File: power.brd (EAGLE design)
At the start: 65 x 56 mm, 7 parts, among them X1 5566-4-RIGHTANGLE, X3 RASPI_BOARD_B+#_H

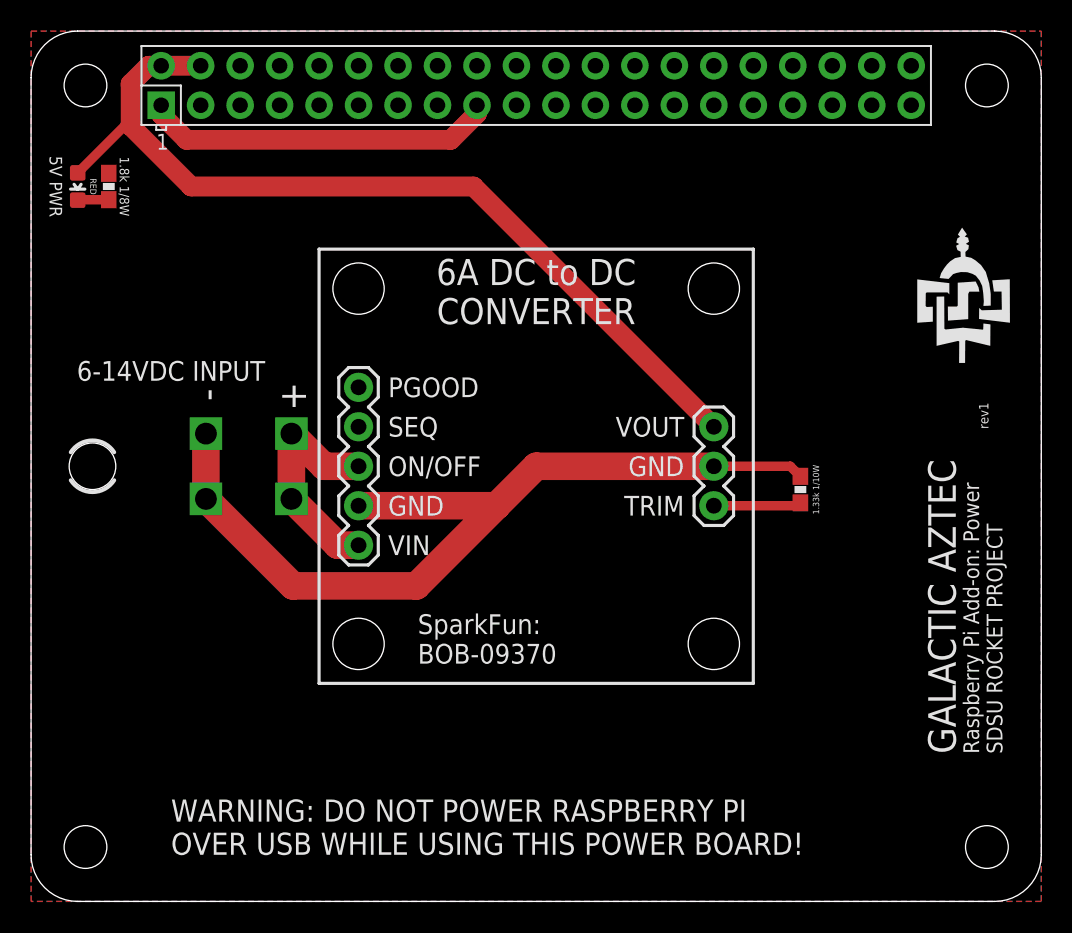
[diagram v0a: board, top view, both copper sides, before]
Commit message: Fix molex connector thru hole size
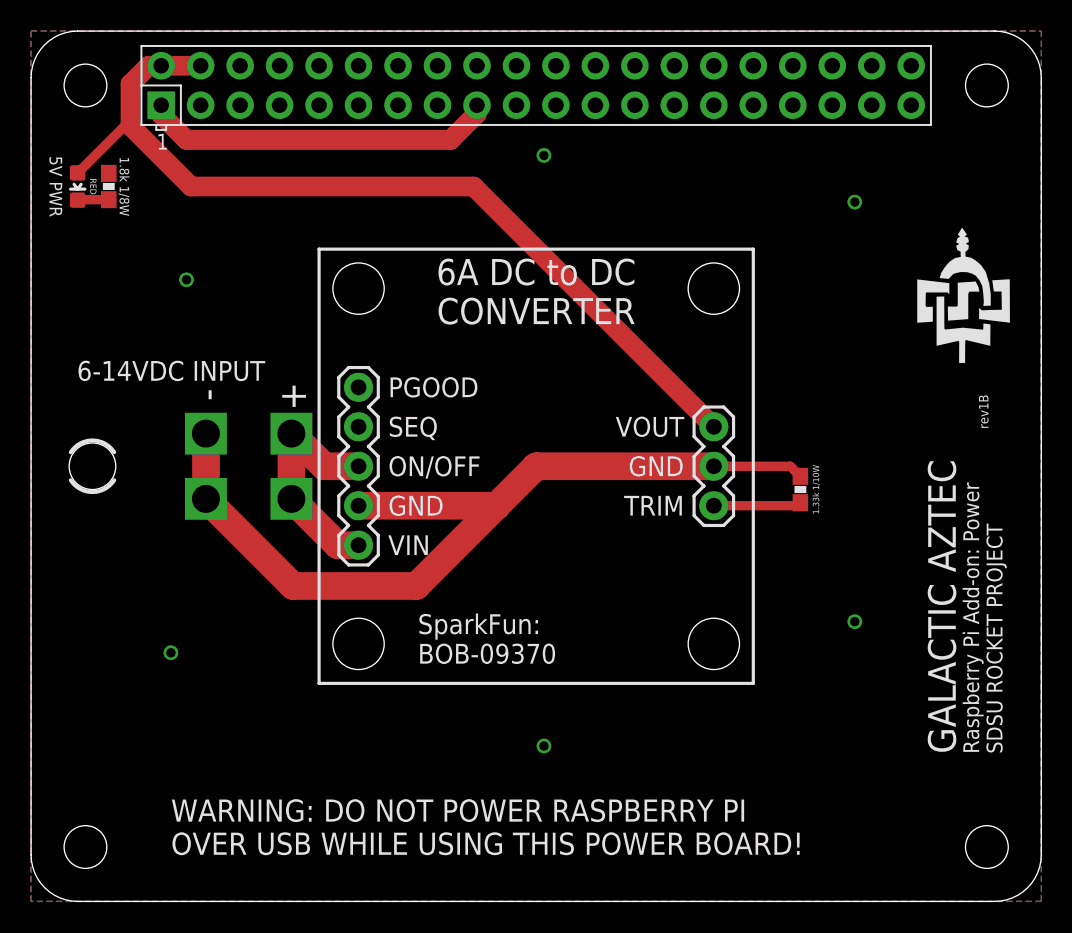
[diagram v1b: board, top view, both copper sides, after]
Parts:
- removed X1: 5566-4-RIGHTANGLE, SDSURocket-BreakoutBoards:5566-4
- added X2: 5566-4-RIGHTANGLE, SDSURocket-Connectors:5566-4
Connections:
- net GND: now also X2.1, X2.2; no longer X1.1, X1.2
- net VIN: now also X2.3, X2.4; no longer X1.3, X1.4
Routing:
- net GND: vias 0 -> 6
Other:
- board text added: "rev1B"
- board text removed: "rev1"
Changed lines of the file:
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@@
 <layer number="56" name="wert" color="7" fill="1" visible="no" active="no"/>
 <layer number="57" name="tCAD" color="7" fill="1" visible="no" active="no"/>
+<layer number="59" name="tCarbon" color="7" fill="1" visible="no" active="no"/>
+<layer number="60" name="bCarbon" color="7" fill="1" visible="no" active="no"/>
 <layer number="90" name="Modules" color="5" fill="1" visible="no" active="no"/>
 <layer number="91" name="Nets" color="2" fill="1" visible="no" active="no"/>
@@
 <layer number="127" name="_tValues" color="7" fill="1" visible="yes" active="yes"/>
 <layer number="128" name="_bValues" color="7" fill="1" visible="yes" active="yes"/>
+<layer number="129" name="Mask" color="7" fill="1" visible="yes" active="yes"/>
 <layer number="131" name="tAdjust" color="7" fill="1" visible="yes" active="yes"/>
 <layer number="132" name="bAdjust" color="7" fill="1" visible="yes" active="yes"/>
@@
 <layer number="251" name="SMDround" color="12" fill="11" visible="no" active="no"/>
 <layer number="254" name="cooling" color="7" fill="1" visible="yes" active="yes"/>
+<layer number="255" name="routoute" color="7" fill="1" visible="yes" active="yes"/>
 </layers>
 <board>
@@
 <text x="61" y="9.5" size="1.016" layer="25" font="vector" ratio="10" rot="R90">Raspberry Pi Add-on: Power</text>
 <text x="62.5" y="9.5" size="1.016" layer="25" font="vector" rot="R90">SDSU ROCKET PROJECT</text>
-<text x="61.6" y="30.4" size="0.6096" layer="25" font="vector" rot="R90">rev1</text>
+<text x="61.6" y="30.4" size="0.6096" layer="25" font="vector" rot="R90">rev1B</text>
 <text x="11.3" y="32.6" size="1.778" layer="25" font="vector" ratio="10" rot="R270" align="center">-</text>
 <text x="16.8" y="32.5" size="1.778" layer="25" font="vector" ratio="10" rot="R270" align="center">+</text>
@@
 <attribute name="DESIGNER" value="NAME" x="0" y="-15" size="1.778" layer="27" font="vector" display="off"/>
 </element>
-<element name="X1" library="SDSURocket-BreakoutBoards" package="5566-4" value="5566-4-RIGHTANGLE" x="14" y="28" smashed="yes" rot="R270">
-<attribute name="OC_NEWARK" value="unknown" x="14" y="28" size="1.778" layer="27" font="vector" rot="R270" display="off"/>
-<attribute name="MPN" value="" x="14" y="28" size="1.778" layer="27" font="vector" rot="R270" display="off"/>
-<attribute name="MF" value="" x="14" y="28" size="1.778" layer="27" font="vector" rot="R270" display="off"/>
-<attribute name="OC_FARNELL" value="unknown" x="14" y="28" size="1.778" layer="27" font="vector" rot="R270" display="off"/>
-</element>
 <element name="D4" library="SparkFun-LED" package="LED-0603" value="RED" x="3" y="46" smashed="yes" rot="R180">
 <attribute name="VALUE" x="3.8" y="46" size="0.4064" layer="25" font="vector" rot="SR270" align="bottom-center"/>
@@
 <element name="R4" library="SparkFun-Resistors" package="0603-RES" value="1.8k 1/8W" x="5" y="46" smashed="yes" rot="R90">
 <attribute name="VALUE" x="5.7" y="46" size="0.6096" layer="25" font="vector" rot="SR270" align="bottom-center"/>
+</element>
+<element name="X2" library="SDSURocket-Connectors" package="5566-4" value="5566-4-RIGHTANGLE" x="14" y="28" smashed="yes" rot="R270">
+<attribute name="OC_NEWARK" value="unknown" x="14" y="28" size="1.778" layer="27" rot="R270" display="off"/>
+<attribute name="MPN" value="" x="14" y="28" size="1.778" layer="27" rot="R270" display="off"/>
+<attribute name="MF" value="" x="14" y="28" size="1.778" layer="27" rot="R270" display="off"/>
+<attribute name="OC_FARNELL" value="unknown" x="14" y="28" size="1.778" layer="27" rot="R270" display="off"/>
 </element>
 </elements>
@@
 <contactref element="R2" pad="2"/>
 <contactref element="R4" pad="2"/>
-<contactref element="X1" pad="1"/>
-<contactref element="X1" pad="2"/>
 <wire x1="21.07" y1="25.46" x2="29.96" y2="25.46" width="1.778" layer="1"/>
 <wire x1="29.96" y1="25.46" x2="32.5" y2="28" width="1.778" layer="1"/>
@@
 <wire x1="11.25" y1="25.9" x2="16.85" y2="20.3" width="1.778" layer="1"/>
 <wire x1="16.85" y1="20.3" x2="24.8" y2="20.3" width="1.778" layer="1"/>
+<via x="33" y="48" extent="1-16" drill="0.6" shape="square"/>
+<via x="53" y="45" extent="1-16" drill="0.6" shape="square"/>
+<via x="53" y="18" extent="1-16" drill="0.6" shape="square"/>
+<via x="33" y="10" extent="1-16" drill="0.6" shape="square"/>
+<via x="9" y="16" extent="1-16" drill="0.6" shape="square"/>
+<via x="10" y="40" extent="1-16" drill="0.6" shape="square"/>
+<contactref element="X2" pad="1"/>
+<contactref element="X2" pad="2"/>
 </signal>
 <signal name="VIN">
 <contactref element="U$1" pad="VIN"/>
-<contactref element="X1" pad="4"/>
-<contactref element="X1" pad="3"/>
 <wire x1="16.75" y1="30.1" x2="16.75" y2="25.9" width="1.778" layer="1"/>
 <wire x1="16.75" y1="25.9" x2="19.73" y2="22.92" width="1.778" layer="1"/>
@@
 <wire x1="16.75" y1="30.1" x2="18.85" y2="28" width="1.778" layer="1"/>
 <wire x1="18.85" y1="28" x2="21.07" y2="28" width="1.778" layer="1"/>
+<contactref element="X2" pad="4"/>
+<contactref element="X2" pad="3"/>
 </signal>
 <signal name="5V">

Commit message: Add DC to DC converter and ideal safety diode
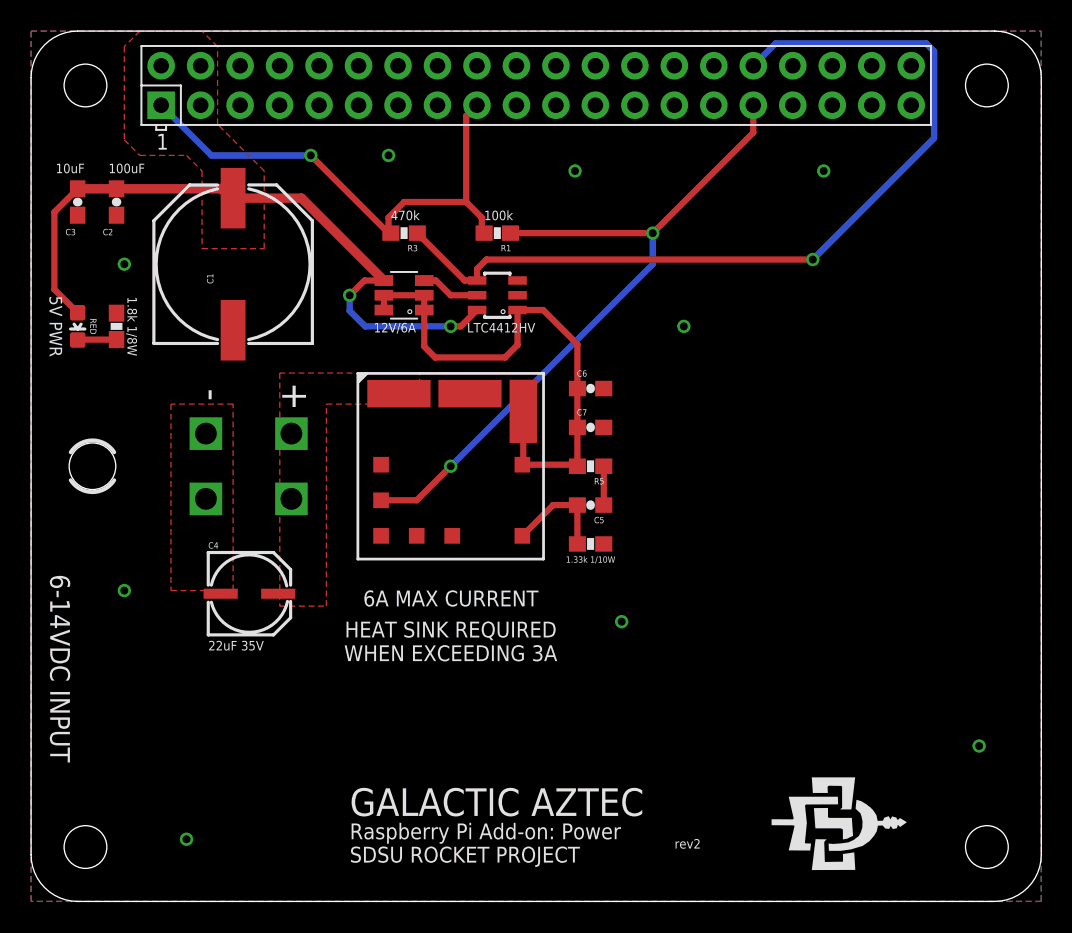
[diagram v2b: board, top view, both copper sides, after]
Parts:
- removed U$1: SFE-DCDC-CONVERTER-BREAKOUT, RocketProject:SFE-DCDC-CONVERTER
- removed X2: 5566-4-RIGHTANGLE, SDSURocket-Connectors:5566-4
- added C1: 800uF, SparkFun-Capacitors:PANASONIC_G
- added C2: 100uF, SparkFun-Capacitors:0603-CAP
- added C3: 10uF, SparkFun-Capacitors:0603-CAP
- added C4: 22uF 35V, SparkFun-Capacitors:PANASONIC_C
- added C5: 3900pF, SparkFun-Capacitors:0603-CAP
- added C6, C7: 47uF, SparkFun-Capacitors:0603-CAP
- added Q1: 12V/6A, SDSURocket-PowerIC:SSOT-6L
- added R1: 100k, SparkFun-Resistors:0603-RES
- added R3: 470k, SparkFun-Passives:0603-RES
- added R5: 220, SparkFun-Passives:0603-RES
- added U$2: DC-DC_CONVERTER, SparkFun-PowerIC:DC-DC_CONVERTER
- added U1: LTC4412HV, SDSURocket-PowerIC:SOT23-6
- added X1: 5566-4-RIGHTANGLE, SDSURocket-BreakoutBoards:5566-4
- moved R2 13.9 mm to (36.0, 23.0), turned to 0 degrees
- moved R4 9.01 mm to (5.50, 37.0)
- moved D4 9.00 mm to (3.00, 37.0)
- moved FRAME1 3.00 mm to (0.00, -18.0)
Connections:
- new net BATT: C6.1, C7.1, Q1.1, Q1.2, Q1.5, Q1.6, R5.2, U$2.4, U$2.5, U1.1
- new net N$1: Q1.3, U1.5
- new net N$2: C5.1, R5.1
- new net WIPI22: R1.1, U$2.10, X3.31
- new net WIPI26: R3.1, U1.4, X3.32
- net 3.3V: now also R1.2, R3.2
- net 5V: now also C1.+, C2.1, C3.1, Q1.4, U1.6; no longer U$1.VOUT
- net GND: now also C1.-, C2.2, C3.2, C4.-, C6.2, C7.2, U$2.3, U$2.7, U1.2, U1.3, X1.1, X1.2; no longer U$1.GND@1, U$1.GND@2, X2.1, X2.2
- net TRIM: now also C5.2, U$2.6; no longer U$1.TRIM
- net VIN: now also C4.+, U$2.2, X1.3, X1.4; no longer U$1.ON/OFF, U$1.VIN, X2.3, X2.4
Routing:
- net GND: track 57.1 -> 0.00 mm, vias 6 -> 8
- net WIPI26: track 0.00 -> 56.8 mm, vias 0 -> 1
- net WIPI22: track 0.00 -> 45.8 mm, vias 0 -> 2
- net BATT: track 0.00 -> 35.4 mm
- net VIN: track 14.9 -> 0.00 mm
- net 5V: track 57.9 -> 44.0 mm, vias 0 -> 2
- net 3.3V: track 22.8 -> 33.7 mm, vias 0 -> 1
- net N$1: track 0.00 -> 3.79 mm
- net N$2: track 0.00 -> 2.50 mm
- net TRIM: track 5.65 -> 6.86 mm
- net N$4: track 2.01 -> 2.51 mm
- added copper zone on layer 1, net 5V
- added copper zone on layer 1, net VIN
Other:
- board text added: "6A MAX CURRENT"
- board text added: "HEAT SINK REQUIRED WHEN EXCEEDING 3A"
- board text added: "rev2"
- board text removed: "WARNING: DO NOT POWER RASPBERRY PI OVER USB WHILE USING THIS POWER BOARD!"
- board text removed: "rev1B"

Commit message: Optimize design and add voltage tuning
Updated design for more capacitor reuse and added additional capacitors
to help stabilize power. Added variable resistor to allow for fine
tuning voltage output. Improved labeling of components on the schematic.
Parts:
- removed C6, C7: 47uF, SparkFun-Capacitors:0603-CAP
- removed X1: 5566-4-RIGHTANGLE, SDSURocket-BreakoutBoards:5566-4
- added CI1: 22uF 16V, SparkFun-Capacitors:NIPPON_F80
- added CI2, CO1, CO2: 47uF 16V, SparkFun-Capacitors:NIPPON_F80
- added RTRIM1: 2k 1/10W, SparkFun-Resistors:0603-RES
- added RTRIM3: 1k 1/10W, SDSURocket-Electromechanical:89P
- added TP1, TP2: TEST-POINT3X5, SparkFun-Passives:PAD.03X.05
- added X2: 5566-4-RIGHTANGLE, SDSURocket-Connectors:5566-4
- C2: value 100uF -> 10uF
- C4: value 22uF 35V -> 10uF; device SparkFun-Capacitors:PANASONIC_C -> SparkFun-Capacitors:0603-CAP
- Q1: value 12V/6A -> 12V 6A
- RTRIM2: value 1.33k 1/10W -> 2.5k 1/10W
- moved C4 23.3 mm to (4.00, 41.0)
- renumbered C5 to CTUNE, R2 to RTRIM2, R5 to RTUNE, U$2 to IC1, U1 to IC2
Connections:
- new net N$3: RTRIM2.2, RTRIM3.1
- net 5V: now also C4.1
- net BATT: now also CO1.+, CO2.+; no longer C6.1, C7.1
- net GND: now also C4.2, CI1.-, CI2.-, CO1.-, CO2.-, RTRIM1.2, RTRIM3.2, TP2.P$1, X2.1, X2.2; no longer C4.-, C6.2, C7.2, RTRIM2.2, X1.1, X1.2
- net TRIM: now also RTRIM1.1, TP1.P$1
- net VIN: now also CI1.+, CI2.+, X2.3, X2.4; no longer C4.+, X1.3, X1.4
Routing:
- net N$3: track 0.00 -> 13.3 mm
- net BATT: track 35.4 -> 43.6 mm
- net TRIM: track 6.86 -> 13.6 mm
- net 5V: track 44.0 -> 45.7 mm
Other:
- board text added: "12VDC RECOMMENDED"
- board text added: "GND TEST POINT"
- board text added: "RTRIM TEST POINT"
- board text added: "rev3"
- board text removed: "rev2"

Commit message: Fix variable resistor thru holes
The thru hole positions and size for the variable resistor (RTRIM3) were
fixed to have the component sit on the top side of the board.
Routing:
- net N$3: track 13.3 -> 15.9 mm
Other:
- board text added: "rev4"
- board text removed: "rev3"
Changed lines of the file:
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@@
 <text x="20.5" y="4" size="1.016" layer="25" font="vector" ratio="10">Raspberry Pi Add-on: Power</text>
 <text x="20.5" y="2.5" size="1.016" layer="25" font="vector">SDSU ROCKET PROJECT</text>
-<text x="41.4" y="3.4" size="0.6096" layer="25" font="vector">rev3</text>
+<text x="41.4" y="3.4" size="0.6096" layer="25" font="vector">rev4</text>
 <text x="11.3" y="32.6" size="1.778" layer="25" font="vector" ratio="10" rot="R270" align="center">-</text>
 <text x="16.8" y="32.5" size="1.778" layer="25" font="vector" ratio="10" rot="R270" align="center">+</text>
@@
 <wire x1="36.85" y1="23" x2="44.92" y2="23" width="0.8128" layer="1"/>
 <wire x1="44.92" y1="23" x2="48.65" y2="26.73" width="0.8128" layer="1"/>
+<wire x1="48.65" y1="26.73" x2="48.65" y2="29.27" width="0.8128" layer="1"/>
 </signal>
 </signals>
